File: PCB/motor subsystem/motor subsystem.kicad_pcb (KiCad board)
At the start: 2 copper layers, 100 x 100 mm, 29 parts, among them U1 MCU_Seeed_XIAO_ESP32-C3, U2 STP55NF06L

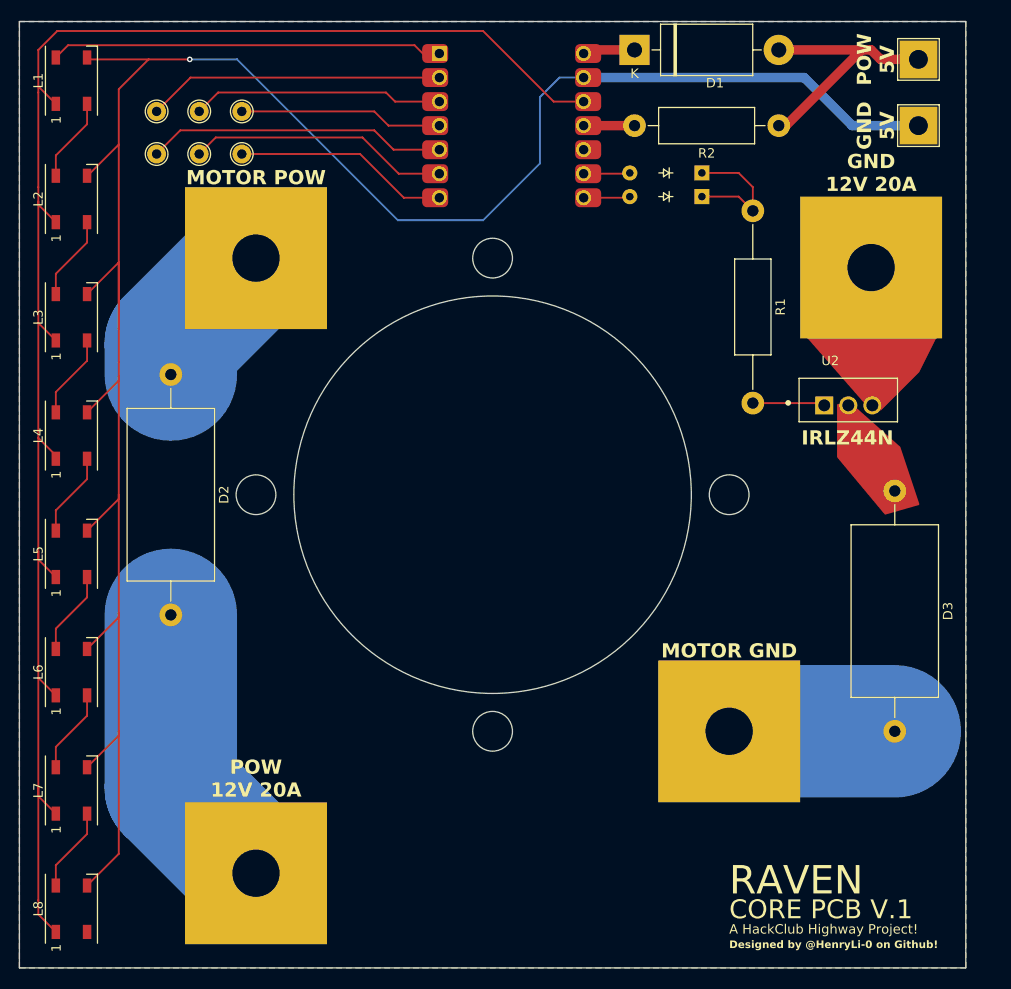
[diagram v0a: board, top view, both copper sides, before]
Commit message: update motor PCB for hall effect sensor and other stuff
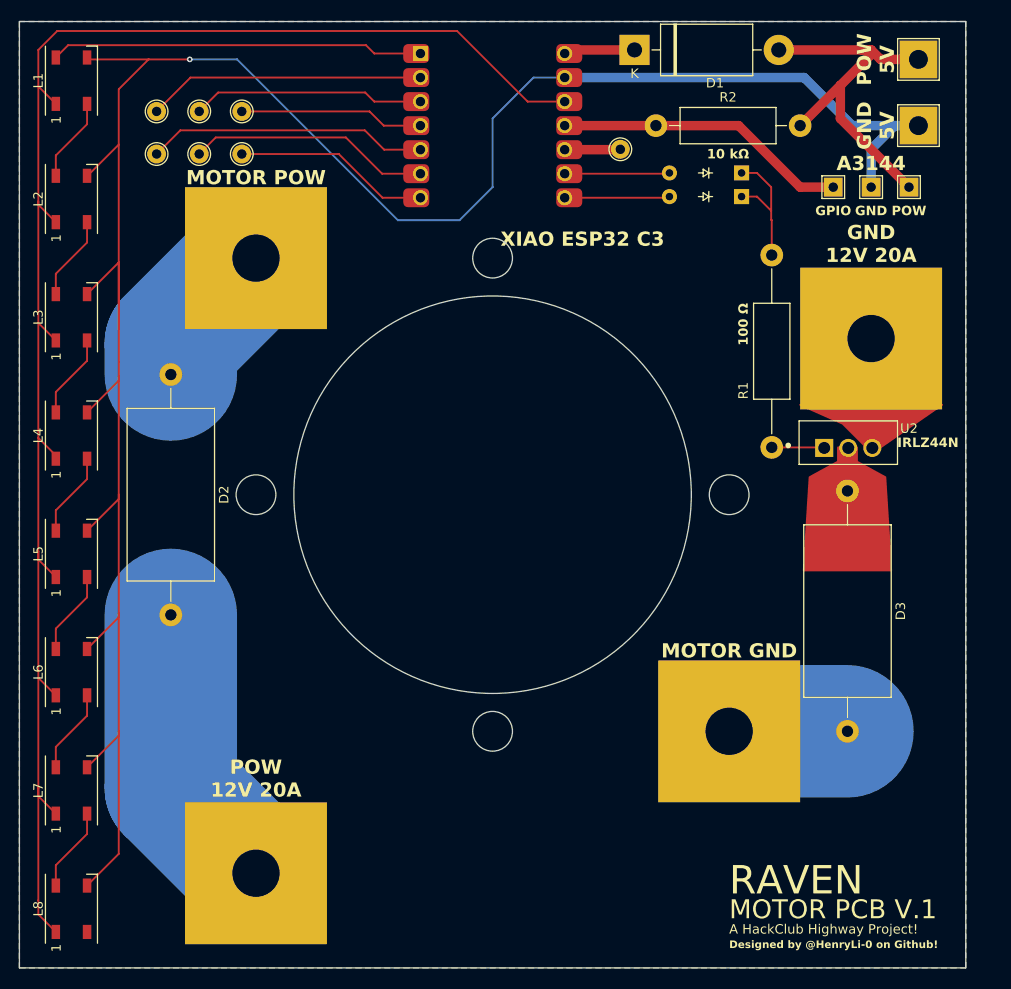
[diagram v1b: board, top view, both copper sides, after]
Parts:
- added REF**: TestPoint_THTPad_2.0x2.0mm_Drill1.0mm, TestPoint:TestPoint_THTPad_2.0x2.0mm_Drill1.0mm, F.Cu at (186.0, 67.5)
- added REF**: TestPoint_THTPad_2.0x2.0mm_Drill1.0mm, TestPoint:TestPoint_THTPad_2.0x2.0mm_Drill1.0mm, F.Cu at (190.0, 67.5)
- added REF**: TestPoint_THTPad_D2.0mm_Drill1.0mm, TestPoint:TestPoint_THTPad_D2.0mm_Drill1.0mm, F.Cu at (163.5, 63.5)
- added REF**: TestPoint_THTPad_2.0x2.0mm_Drill1.0mm, TestPoint:TestPoint_THTPad_2.0x2.0mm_Drill1.0mm, F.Cu at (194.0, 67.5)
- moved ? 7.50 mm to (190.0, 83.5)
- moved R1 5.09 mm to (179.5, 74.7)
- moved D3 5.00 mm to (187.5, 99.6)
- moved U2 4.50 mm to (185.0, 95.1)
- moved D4 4.19 mm to (176.3, 66.0)
- moved D5 4.19 mm to (176.3, 68.5)
- moved R2 2.26 mm to (182.5, 61.0)
- moved U1 2.00 mm to (150.0, 61.0)
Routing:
- net A3144E GPIO: track 5.02 -> 31.1 mm
- net 5V POW: track 27.2 -> 40.0 mm
- net 5V GND: track 234.4 -> 242.1 mm
- net Net-(D4-A): track 5.03 -> 11.1 mm
- net Net-(D5-A): track 5.10 -> 11.1 mm
- net unconnected-(U1-PA5_A9_D9_MISO-Pad10): track 0.00 -> 5.90 mm
- net MOTOR-: track 17.5 -> 12.5 mm
- net unconnected-(U1-PA10_A2_D2-Pad3): track 26.6 -> 24.6 mm
- net Net-(D1-K): track 5.54 -> 7.54 mm
- net LED: track 41.0 -> 39.0 mm
- net +3V3: track 176.2 -> 174.2 mm
- net Net-(R1-Pad2): track 7.31 -> 5.57 mm
- net unconnected-(U1-PB08_A6_D6_TX-Pad7): track 22.3 -> 20.8 mm
- net unconnected-(U1-PA8_A4_D4_SDA-Pad5): track 31.3 -> 29.8 mm
- net unconnected-(U1-PA4_A1_D1-Pad2): track 30.9 -> 29.4 mm
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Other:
- board text added: "10 kΩ"
- board text added: "100 Ω"
- board text added: "A3144"
- board text added: "GND"
- board text added: "GPIO"
- board text added: "MOTOR PCB V.1"
- board text added: "POW"
- board text added: "R1"
- board text added: "U2"
- board text added: "XIAO ESP32 C3"
- board text removed: "CORE PCB V.1"

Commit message: lots of CAD progress!
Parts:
- moved R1 2.18 mm to (179.5, 72.5)
- moved D4 1.29 mm to (175.1, 65.5)
- moved D5 1.29 mm to (175.1, 68.0)
- moved R2 0.50 mm to (182.5, 60.5)
- moved REF** 0.50 mm to (163.5, 63.0)
- moved U1 0.50 mm to (150.0, 60.5)
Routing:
- net Net-(D4-A): track 11.1 -> 9.91 mm
- net Net-(D5-A): track 11.1 -> 9.93 mm
- net Net-(R1-Pad2): track 5.57 -> 6.47 mm
- net Net-(D4-K): track 14.7 -> 15.3 mm

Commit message: 07172025 - wrapping up CAD!
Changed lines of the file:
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@@
 	)
 	(segment
-		(start 136.5 61.5)
-		(end 138.04 63.04)
-		(width 0.2)
-		(layer "F.Cu")
-		(net 20)
-	)
-	(segment
-		(start 138.04 63.04)
-		(end 142.38 63.04)
-		(width 0.2)
-		(layer "F.Cu")
-		(net 20)
-	)
-	(segment
-		(start 117 61.5)
-		(end 136.5 61.5)
+		(start 137 61.5)
+		(end 138.54 63.04)
 		(width 0.2)
 		(layer "F.Cu")
@@
 	)
 	(segment
-		(start 137.83 65.58)
+		(start 138.54 63.04)
+		(end 142.38 63.04)
+		(width 0.2)
+		(layer "F.Cu")
+		(net 20)
+	)
+	(segment
+		(start 117 61.5)
+		(end 137 61.5)
+		(width 0.2)
+		(layer "F.Cu")
+		(net 20)
+	)
+	(segment
+		(start 139.33 65.58)
 		(end 142.38 65.58)
 		(width 0.2)
@@
 	(segment
 		(start 120.75 62.25)
-		(end 134.5 62.25)
+		(end 136 62.25)
 		(width 0.2)
 		(layer "F.Cu")
@@
 	)
 	(segment
-		(start 134.5 62.25)
-		(end 137.83 65.58)
+		(start 136 62.25)
+		(end 139.33 65.58)
 		(width 0.2)
 		(layer "F.Cu")
@@
 	)
 	(segment
-		(start 137.87 68.12)
+		(start 140.12 68.12)
 		(end 142.38 68.12)
 		(width 0.2)
@@
 	)
 	(segment
-		(start 133.75 64)
-		(end 137.87 68.12)
+		(start 123.5 64)
+		(end 136 64)
 		(width 0.2)
 		(layer "F.Cu")
@@
 	)
 	(segment
-		(start 123.5 64)
-		(end 133.75 64)
+		(start 136 64)
+		(end 140.12 68.12)
 		(width 0.2)
 		(layer "F.Cu")
@@
 	)
 	(segment
-		(start 119 59.5)
-		(end 121 57.5)
+		(start 121 57.5)
+		(end 137 57.5)
 		(width 0.2)
 		(layer "F.Cu")
@@
 	)
 	(segment
-		(start 137 57.96)
+		(start 137 57.5)
+		(end 137.46 57.96)
+		(width 0.2)
+		(layer "F.Cu")
+		(net 23)
+	)
+	(segment
+		(start 137.46 57.96)
 		(end 142.38 57.96)
 		(width 0.2)
@@
 	)
 	(segment
-		(start 121 57.5)
-		(end 136.54 57.5)
-		(width 0.2)
-		(layer "F.Cu")
-		(net 23)
-	)
-	(segment
-		(start 136.54 57.5)
-		(end 137 57.96)
+		(start 119 59.5)
+		(end 121 57.5)
 		(width 0.2)
 		(layer "F.Cu")
@@
 	)
 	(segment
-		(start 114.5 59.5)
-		(end 118.58 55.42)
+		(start 137 56)
+		(end 137.58 55.42)
 		(width 0.2)
 		(layer "F.Cu")
@@
 	)
 	(segment
-		(start 118.58 55.42)
+		(start 137.58 55.42)
 		(end 142.38 55.42)
 		(width 0.2)
 		(layer "F.Cu")
+		(net 25)
+	)
+	(segment
+		(start 114.5 59.5)
+		(end 118 56)
+		(width 0.2)
+		(layer "F.Cu")
+		(net 25)
+	)
+	(segment
+		(start 118 56)
+		(end 137 56)
+		(width 0.2)
+		(layer "F.Cu")

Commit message: mosfet nightmares and cad
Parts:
- removed L7, L8: LED_WS2812B, ScottoKeebs_Components:LED_WS2812B
- added G***: LOGO, LOGO, F.Cu at (162.5, 143.5)
- added G***: LOGO, LOGO, F.Cu at (152.5, 143.7)
- added G***: LOGO, LOGO, B.Cu at (152.5, 143.7)
- added G***: LOGO, LOGO, B.Cu at (162.5, 143.5)
- U2: value STP55NF06L -> IRLZ44N
- moved L1 12.8 mm to (105.5, 69.0)
- moved L2 12.8 mm to (105.5, 81.5)
- moved L3 12.8 mm to (105.5, 94.0)
- moved L4 12.8 mm to (105.5, 106.5)
- moved L5 12.8 mm to (105.5, 119.0)
- moved L6 12.8 mm to (105.5, 131.5)
- moved REF** 8.00 mm to (187.0, 54.0)
- moved REF** 8.00 mm to (187.0, 61.0)
- moved D1 2.50 mm to (162.5, 53.0)
- moved REF** 1.50 mm to (125.0, 59.5)
- moved REF** 1.50 mm to (125.0, 64.0)
- moved R2 1.26 mm to (181.2, 60.5)
- moved REF** 1.00 mm to (120.0, 59.5)
- moved REF** 1.00 mm to (162.5, 63.0)
- moved REF** 1.00 mm to (120.0, 64.0)
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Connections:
- L6 pad 2: Net-(L6-DOUT) -> unconnected-(L6-DOUT-Pad2)
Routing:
- net 5V GND: track 242.5 -> 214.1 mm
- net +3V3: track 174.0 -> 148.7 mm
- net Net-(L7-DOUT): track 8.97 -> 0.00 mm
- net Net-(L6-DOUT): track 8.97 -> 0.00 mm
- net LED: track 39.2 -> 45.6 mm
- net 5V POW: track 39.8 -> 33.7 mm
- net Net-(D1-K): track 7.43 -> 4.93 mm
- net unconnected-(U1-PB08_A6_D6_TX-Pad7): track 20.6 -> 19.1 mm
- net unconnected-(U1-PA11_A3_D3-Pad4): track 19.3 -> 17.8 mm
- net unconnected-(U1-PA10_A2_D2-Pad3): track 24.4 -> 23.4 mm
- net unconnected-(U1-PA9_A5_D5_SCL-Pad6): track 25.5 -> 24.5 mm
- net unconnected-(U1-PA5_A9_D9_MISO-Pad10): track 5.90 -> 4.90 mm
- net unconnected-(U1-PA8_A4_D4_SDA-Pad5): track 29.6 -> 29.1 mm
- net unconnected-(U1-PA4_A1_D1-Pad2): track 29.6 -> 29.1 mm
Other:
- outline, holes or cut-outs redrawn
- board text added: "5V"
- board text removed: "GND 5V"
- board text removed: "POW 5V"

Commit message: 07222025 - checks and a MOSFET!
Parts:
- moved D2 22.3 mm to (116.0, 109.6)
- moved ? 12.5 mm to (137.5, 140.0)
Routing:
- net MOTOR+: track 16.0 -> 38.8 mm
- net 12V @20A POW: track 31.0 -> 23.6 mm

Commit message: 07232025 - mosfet added and writing BOM!
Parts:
- added R3: Resistor, Resistor_THT:R_Axial_DIN0411_L9.9mm_D3.6mm_P15.24mm_Horizontal, F.Cu at (181.5, 72.5)
- R1: footprint Resistor_THT:R_Axial_DIN0411_L9.9mm_D3.6mm_P20.32mm_Horizontal -> Resistor_THT:R_Axial_DIN0411_L9.9mm_D3.6mm_P12.70mm_Horizontal
- U2: value IRLZ44N -> ~; footprint STP55NF06L:TO254P1040X460X1935-3 -> STP55NF06L:AOD424
- moved D3 5.39 mm to (189.5, 104.6)
- moved U2 5.19 mm to (189.5, 97.7), turned to 180 degrees
- moved R1 4.30 mm to (179.5, 76.8)
- moved ? 1.00 mm to (191.0, 83.5)
- moved D4 0.31 mm to (174.8, 65.5)
- moved D5 0.31 mm to (174.8, 68.0)
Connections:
- net A3144E GPIO renamed HALL GPIO
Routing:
- net 5V GND: track 214.1 -> 234.9 mm
- net Net-(R1-Pad2): track 6.47 -> 22.9 mm, vias 0 -> 1
- net Net-(D4-K): track 15.3 -> 26.8 mm
- net MOTOR-: track 12.5 -> 18.2 mm
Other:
- board text added: "12V 20A GND"
- board text added: "12V 20A POW"
- board text removed: "GND 12V 20A"
- board text removed: "IRLZ44N"
- board text removed: "POW 12V 20A"

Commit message: motor pcb edits
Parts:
- added D6: 30SQ045, Resistor_THT:R_Axial_DIN0918_L18.0mm_D9.0mm_P25.40mm_Horizontal, F.Cu at (124.0, 116.5)
- added G***: LOGO, LOGO, F.Cu at (178.6, 123.1)
- added G***: LOGO, LOGO, B.Cu at (178.6, 123.1)
- moved ? 20.0 mm to (117.5, 141.0)
- moved G*** 20.0 mm to (142.5, 143.5) (x2)
- moved G*** 20.0 mm to (132.5, 143.7) (x2)
- moved ? 16.5 mm to (179.0, 141.0)
- moved ? 5.00 mm to (120.0, 75.0)
- moved D2 4.37 mm to (114.5, 105.5)
- moved D3 3.91 mm to (192.5, 107.1)
- moved U2 3.63 mm to (192.5, 99.8), turned to -90 degrees
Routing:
- net MOTOR-: track 18.2 -> 56.8 mm
- net 5V GND: track 234.9 -> 218.8 mm
- net 12V @20A POW: track 23.6 -> 9.14 mm
- net MOTOR+: track 38.8 -> 47.7 mm
- net Net-(R1-Pad2): track 22.9 -> 20.1 mm
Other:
- board text added: ">>>>>>>|"
- board text added: "AOD424"
- board text added: "OMG MOTOR"
- board text added: "R3"
- board text added: "move into the light..."

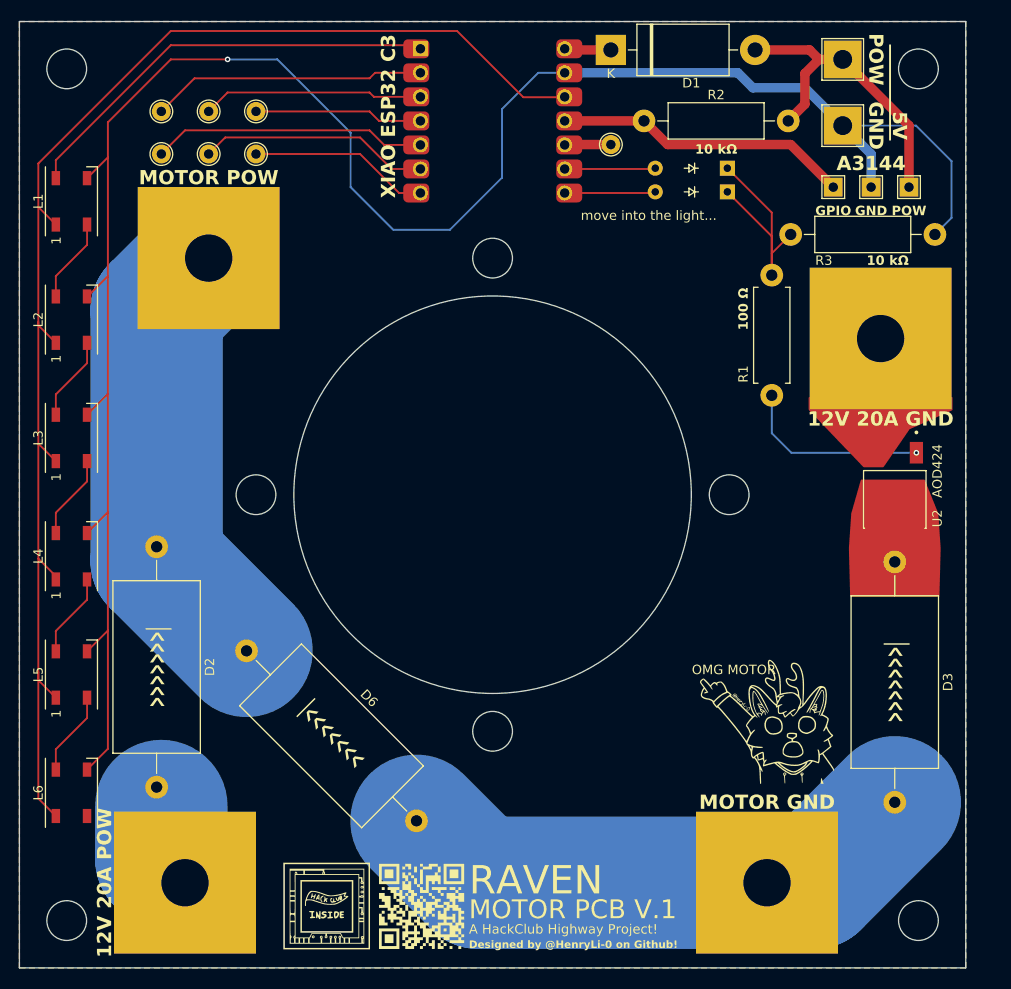
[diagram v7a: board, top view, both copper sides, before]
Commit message: 07242025 - parts and almost finishing BOM!
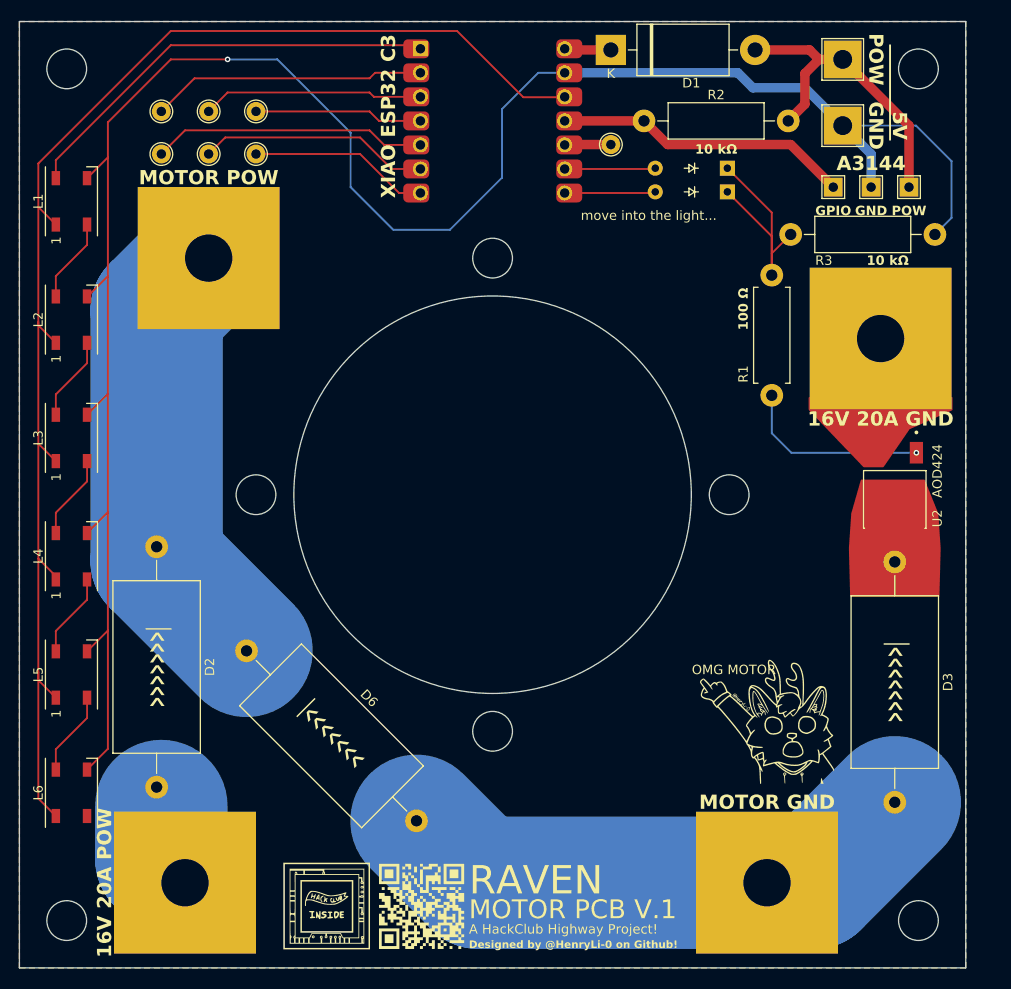
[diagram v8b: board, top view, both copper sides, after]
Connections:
- net 12V @20A GND renamed 16V @20A GND
- net 12V @20A POW renamed 16V @20A POW
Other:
- board text added: "16V 20A GND"
- board text added: "16V 20A POW"
- board text removed: "12V 20A GND"
- board text removed: "12V 20A POW"
